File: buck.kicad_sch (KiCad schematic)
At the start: 35 parts, among them J6 Conn_01x02_Socket, Q3 BSC059N04LS6, Q4 BSC059N04LS6, U6 BQ24640

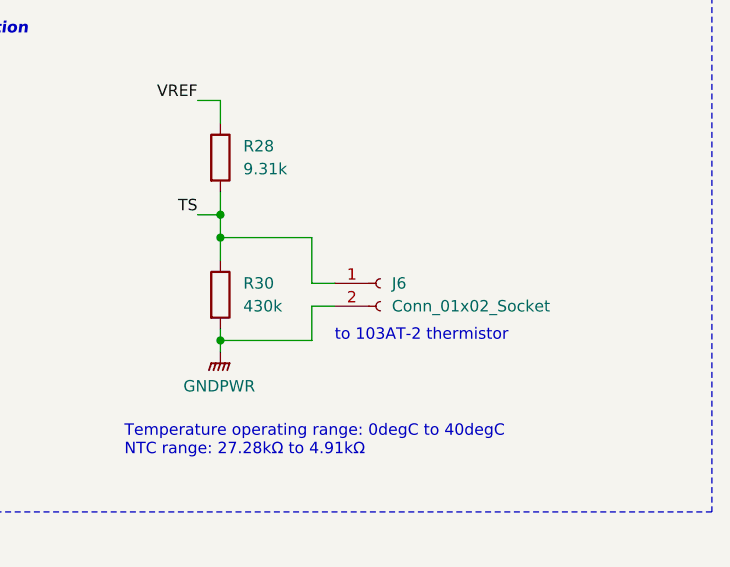
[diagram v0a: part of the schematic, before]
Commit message: Renumbering components
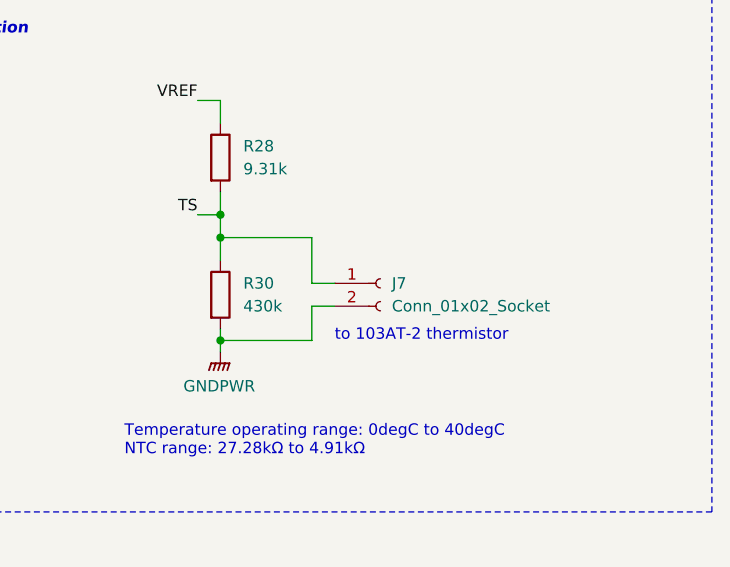
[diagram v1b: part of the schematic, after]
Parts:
- renumbered J6 to J7
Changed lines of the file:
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@@
 		(dnp no)
 		(fields_autoplaced yes)
-		(property "Reference" "#PWR035"
+		(property "Reference" "#PWR037"
 			(at 193.04 86.36 0)
 			(effects
@@
 			(project "SupercapManager"
 				(path "/6197145b-e7d4-44cc-9d90-537b6501bf60/388608c4-ca49-4b14-9684-8f150e280879"
-					(reference "#PWR035")
+					(reference "#PWR037")
 					(unit 1)
 				)
@@
 		(dnp no)
 		(fields_autoplaced yes)
-		(property "Reference" "#PWR040"
+		(property "Reference" "#PWR042"
 			(at 95.25 102.87 0)
 			(effects
@@
 			(project "SupercapManager"
 				(path "/6197145b-e7d4-44cc-9d90-537b6501bf60/388608c4-ca49-4b14-9684-8f150e280879"
-					(reference "#PWR040")
+					(reference "#PWR042")
 					(unit 1)
 				)
@@
 		(dnp no)
 		(fields_autoplaced yes)
-		(property "Reference" "#PWR043"
+		(property "Reference" "#PWR045"
 			(at 123.19 151.13 0)
 			(effects
@@
 			(project "SupercapManager"
 				(path "/6197145b-e7d4-44cc-9d90-537b6501bf60/388608c4-ca49-4b14-9684-8f150e280879"
-					(reference "#PWR043")
+					(reference "#PWR045")
 					(unit 1)
 				)
@@
 		(dnp no)
 		(fields_autoplaced yes)
-		(property "Reference" "#PWR042"
+		(property "Reference" "#PWR044"
 			(at 226.06 148.59 0)
 			(effects
@@
 			(project "SupercapManager"
 				(path "/6197145b-e7d4-44cc-9d90-537b6501bf60/388608c4-ca49-4b14-9684-8f150e280879"
-					(reference "#PWR042")
+					(reference "#PWR044")
 					(unit 1)
 				)
@@
 		(dnp no)
 		(fields_autoplaced yes)
-		(property "Reference" "#PWR041"
+		(property "Reference" "#PWR043"
 			(at 67.31 135.89 0)
 			(effects
@@
 			(project ""
 				(path "/6197145b-e7d4-44cc-9d90-537b6501bf60/388608c4-ca49-4b14-9684-8f150e280879"
-					(reference "#PWR041")
+					(reference "#PWR043")
 					(unit 1)
 				)
@@
 		(dnp no)
 		(fields_autoplaced yes)
-		(property "Reference" "J6"
+		(property "Reference" "J7"
 			(at 245.11 135.8899 0)
 			(effects
@@
 			(project ""
 				(path "/6197145b-e7d4-44cc-9d90-537b6501bf60/388608c4-ca49-4b14-9684-8f150e280879"
-					(reference "J6")
+					(reference "J7")
 					(unit 1)
 				)
@@
 		(dnp no)
 		(fields_autoplaced yes)
-		(property "Reference" "#PWR038"
+		(property "Reference" "#PWR040"
 			(at 46.99 100.33 0)
 			(effects
@@
 			(project "SupercapManager"
 				(path "/6197145b-e7d4-44cc-9d90-537b6501bf60/388608c4-ca49-4b14-9684-8f150e280879"
-					(reference "#PWR038")
+					(reference "#PWR040")
 					(unit 1)
 				)
@@
 		(dnp no)
 		(fields_autoplaced yes)
-		(property "Reference" "#PWR039"
+		(property "Reference" "#PWR041"
 			(at 232.41 101.6 0)
 			(effects
@@
 			(project "SupercapManager"
 				(path "/6197145b-e7d4-44cc-9d90-537b6501bf60/388608c4-ca49-4b14-9684-8f150e280879"
-					(reference "#PWR039")
+					(reference "#PWR041")
 					(unit 1)
 				)
@@
 		(dnp no)
 		(fields_autoplaced yes)
-		(property "Reference" "#PWR033"
+		(property "Reference" "#PWR035"
 			(at 127 52.07 0)
 			(effects
@@
 			(project "SupercapManager"
 				(path "/6197145b-e7d4-44cc-9d90-537b6501bf60/388608c4-ca49-4b14-9684-8f150e280879"
-					(reference "#PWR033")
+					(reference "#PWR035")
 					(unit 1)
 				)
@@
 		(dnp no)
 		(fields_autoplaced yes)
-		(property "Reference" "#PWR034"
+		(property "Reference" "#PWR036"
 			(at 41.91 55.88 0)
 			(effects
@@
 			(project "SupercapManager"
 				(path "/6197145b-e7d4-44cc-9d90-537b6501bf60/388608c4-ca49-4b14-9684-8f150e280879"
-					(reference "#PWR034")
+					(reference "#PWR036")
 					(unit 1)
 				)
@@
 		(dnp no)
 		(fields_autoplaced yes)
-		(property "Reference" "#PWR037"
+		(property "Reference" "#PWR039"
 			(at 176.53 88.9 0)
 			(effects
@@
 			(project "SupercapManager"
 				(path "/6197145b-e7d4-44cc-9d90-537b6501bf60/388608c4-ca49-4b14-9684-8f150e280879"
-					(reference "#PWR037")
+					(reference "#PWR039")
 					(unit 1)
 				)
@@
 		(dnp no)
 		(fields_autoplaced yes)
-		(property "Reference" "#PWR036"
+		(property "Reference" "#PWR038"
 			(at 148.59 88.9 0)
 			(effects
@@
 			(project "SupercapManager"
 				(path "/6197145b-e7d4-44cc-9d90-537b6501bf60/388608c4-ca49-4b14-9684-8f150e280879"
-					(reference "#PWR036")
+					(reference "#PWR038")
 					(unit 1)
 				)

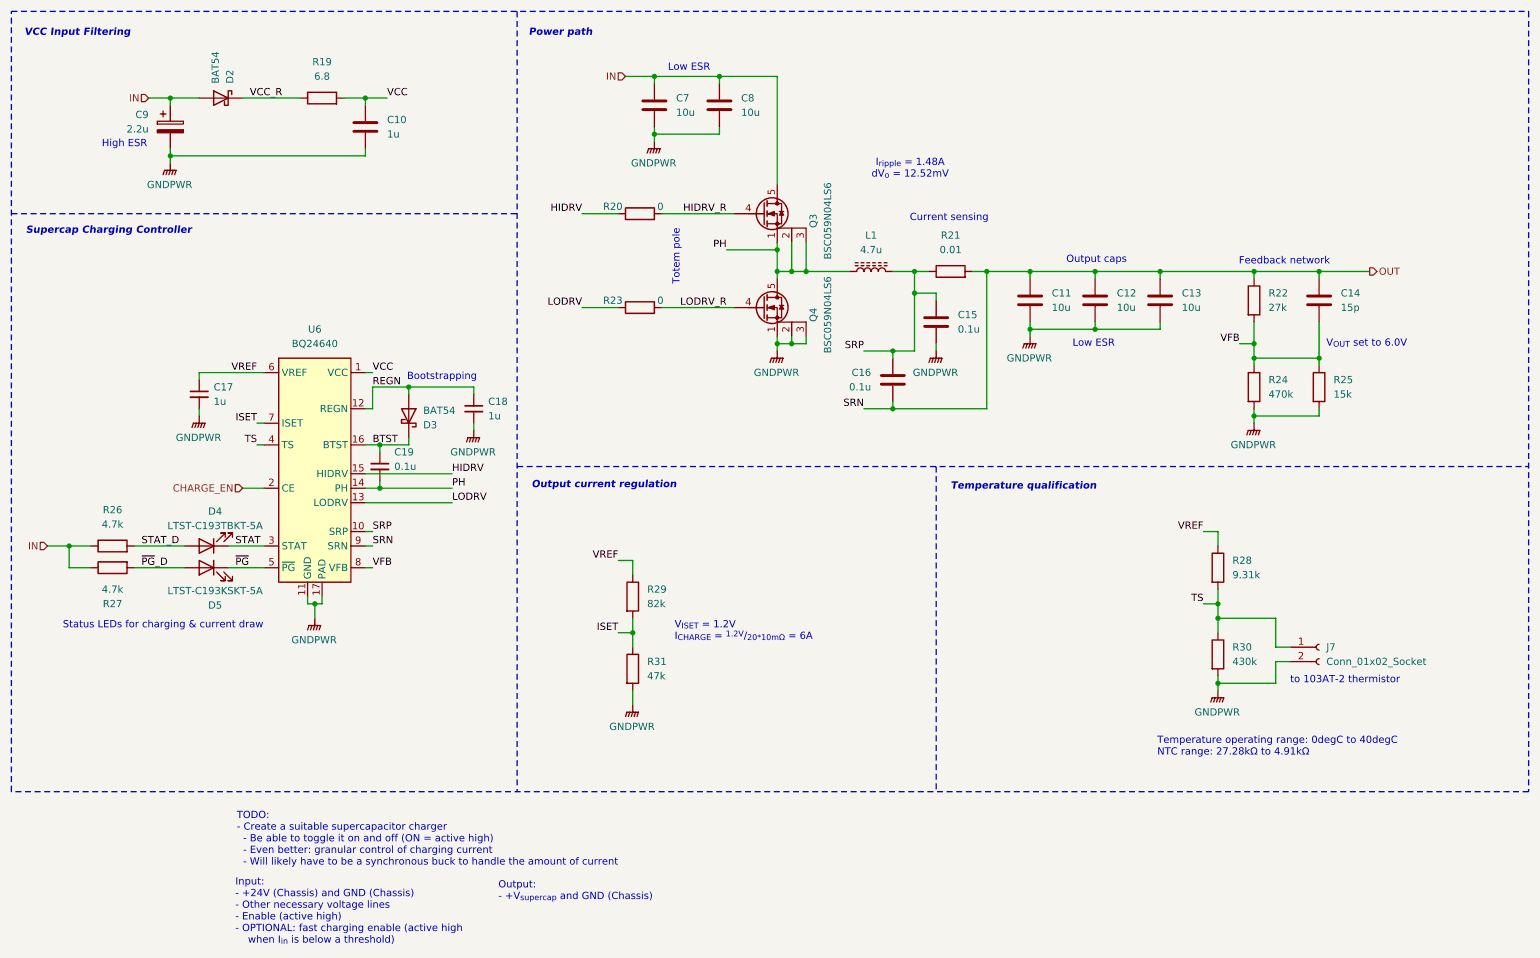
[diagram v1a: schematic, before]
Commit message: Add voltage ratings to capacitors & respec caps to not explode
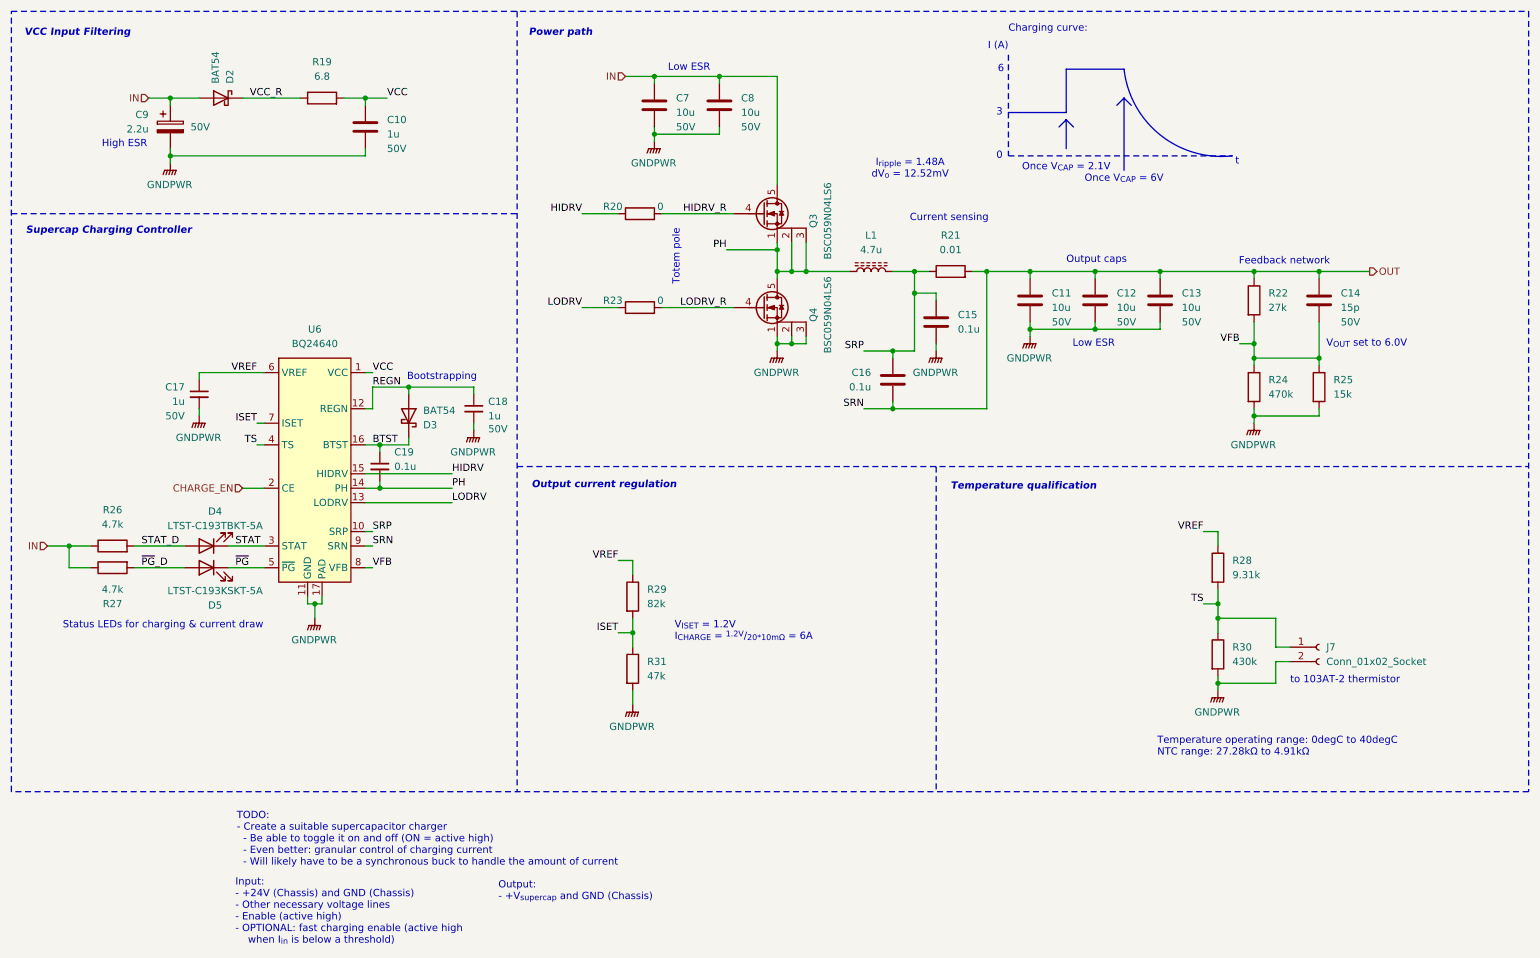
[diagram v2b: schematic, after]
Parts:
- C10, C17, C18: Mouser Part Number 80-C0603C105K9PLR -> 963-UMK107BJ105KA-T; Voltage Rating (none) -> 50V
- C11, C12, C13, C7, C8: footprint Capacitor_SMD:C_0805_2012Metric_Pad1.18x1.45mm_HandSolder -> Capacitor_SMD:C_1206_3216Metric_Pad1.33x1.80mm_HandSolder; Mouser Part Number 187-CL21A106KAYNNNE -> 187-CL31A106KBHNNNE; Voltage Rating (none) -> 50V
- C14, C9: Voltage Rating (none) -> 50V
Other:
- note added: "0"
- note added: "3"
- note added: "6"
- note added: "Charging curve:"
- note added: "I (A)"
- note added: "Once V_{CAP} = 2.1V"
- note added: "Once V_{CAP} = 6V"
- note added: "t"

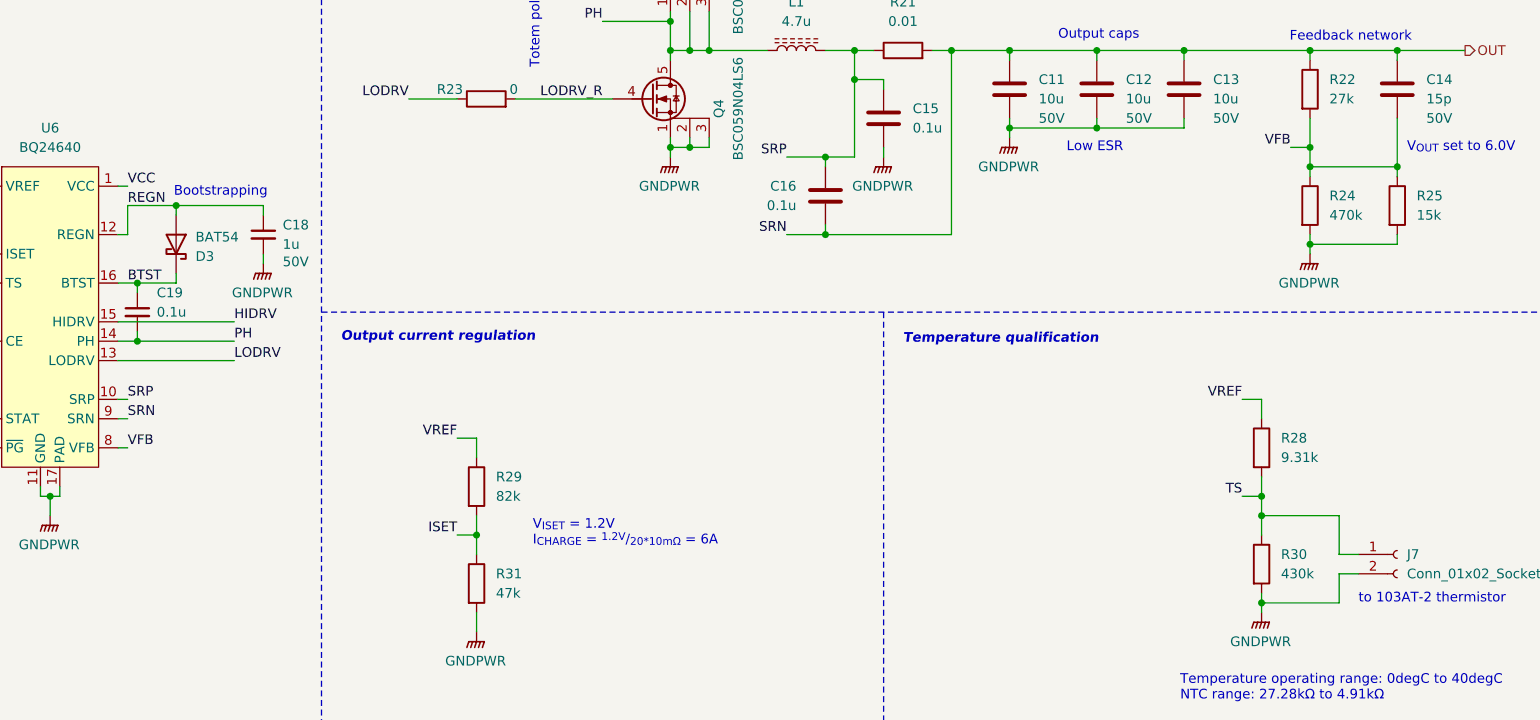
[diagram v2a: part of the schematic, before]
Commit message: Specc'd all components + started creating rev 1b boards
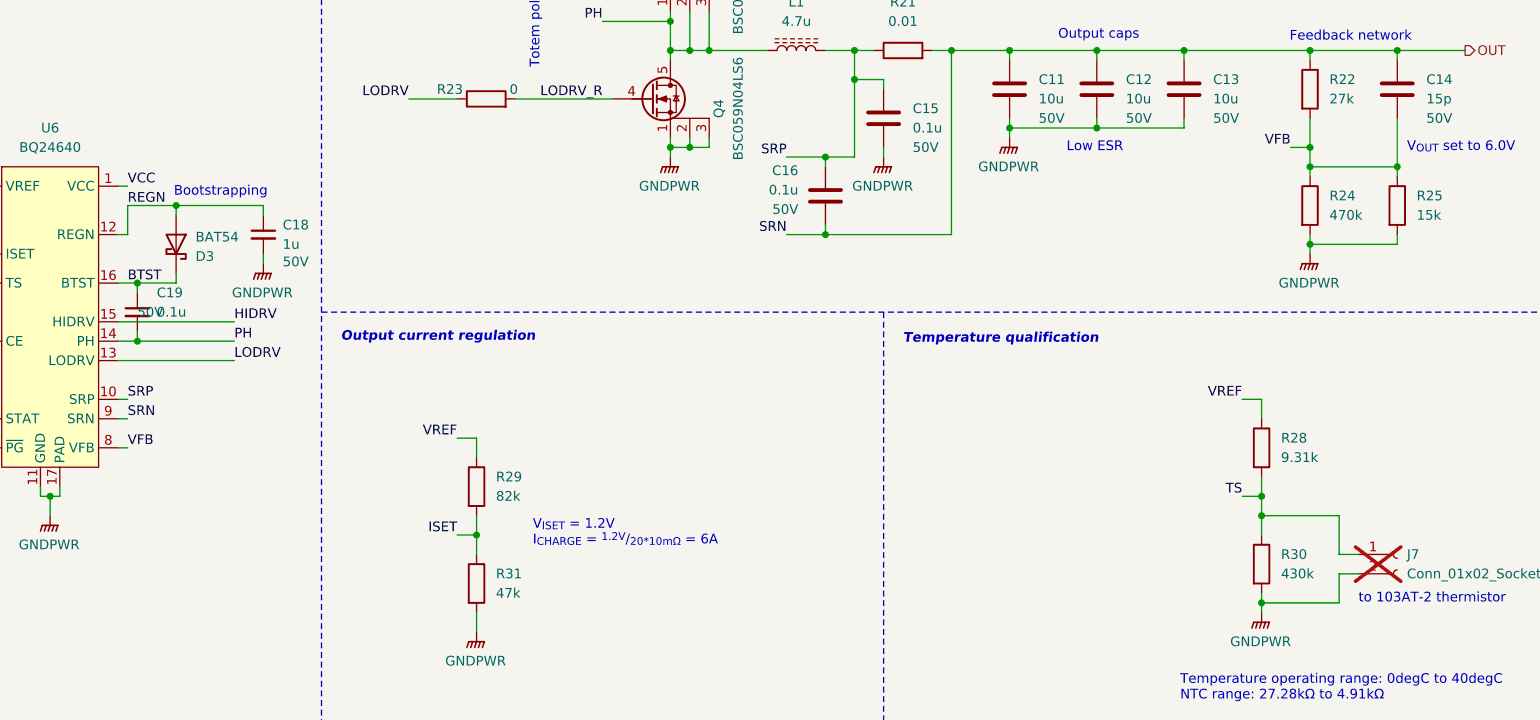
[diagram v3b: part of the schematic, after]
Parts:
- C15, C16, C19: Mouser Part Number (none) -> 581-KGM15BR71H104JT; Voltage Rating (none) -> 50V
- J7: now not fitted
- R19: footprint Resistor_SMD:R_0603_1608Metric_Pad0.98x0.95mm_HandSolder -> Resistor_SMD:R_0805_2012Metric_Pad1.20x1.40mm_HandSolder; Mouser Part Number (none) -> 660-RK73B2ATTD6R8J
- R20, R23: Mouser Part Number (none) -> 660-RK73Z1JTTDD
- R22: Mouser Part Number 667-ERA-3AEB204V -> 660-RN73H1JTD2702B25
- R24: Mouser Part Number 603-RT0603BRD07280KL -> 660-RN73R1JTD4703B25
- R25: Mouser Part Number 603-RC0603FR-071M05L -> 603-RT0603FRE1315KL
- R26, R27: Mouser Part Number 603-RT0603FRE133K6L -> 660-RN73R1JTD4701F50
- R28: Mouser Part Number (none) -> 603-RT0603DRE079K31L
- R29: Mouser Part Number (none) -> 603-RT0603FRE0782KL
- R30: Mouser Part Number (none) -> 603-RT0603FRE07430KL
- R31: Mouser Part Number (none) -> 603-RC0603FR-1047KL
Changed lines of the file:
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@@
 			)
 		)
-		(property "Mouser Part Number" "667-ERA-3AEB204V"
+		(property "Mouser Part Number" "660-RN73H1JTD2702B25"
 			(at 232.41 74.93 0)
 			(effects
@@
 			)
 		)
+		(property "Mouser Part Number" "603-RT0603FRE07430KL"
+			(at 226.06 137.16 0)
+			(effects
+				(font
+					(size 1.27 1.27)
+				)
+				(hide yes)
+			)
+		)
 		(pin "1"
 		)
@@
 			)
 		)
+		(property "Mouser Part Number" "660-RK73Z1JTTDD"
+			(at 124.46 59.69 0)
+			(effects
+				(font
+					(size 1.27 1.27)
+				)
+				(hide yes)
+			)
+		)
 		(pin "2"
 		)
@@
 			)
 		)
-		(property "Footprint" "Resistor_SMD:R_0603_1608Metric_Pad0.98x0.95mm_HandSolder"
+		(property "Footprint" "Resistor_SMD:R_0805_2012Metric_Pad1.20x1.40mm_HandSolder"
 			(at 68.58 41.148 90)
 			(effects
@@
 			)
 		)
+		(property "Mouser Part Number" "660-RK73B2ATTD6R8J"
+			(at 68.58 39.37 0)
+			(effects
+				(font
+					(size 1.27 1.27)
+				)
+				(hide yes)
+			)
+		)
 		(pin "1"
 		)
@@
 			)
 		)
-		(property "Mouser Part Number" "603-RT0603FRE133K6L"
+		(property "Mouser Part Number" "660-RN73R1JTD4701F50"
 			(at 31.75 121.92 0)
 			(effects
@@
 			)
 		)
-		(property "Mouser Part Number" "603-RC0603FR-071M05L"
+		(property "Mouser Part Number" "603-RT0603FRE1315KL"
 			(at 243.84 90.17 0)
 			(effects
@@
 			)
 		)
+		(property "Mouser Part Number" "660-RK73Z1JTTDD"
+			(at 124.46 76.2 0)
+			(effects
+				(font
+					(size 1.27 1.27)
+				)
+				(hide yes)
+			)
+		)
 		(pin "2"
 		)
@@
 		(in_bom yes)
 		(on_board yes)
-		(dnp no)
+		(dnp yes)
 		(fields_autoplaced yes)
 		(property "Reference" "J7"
@@
 			)
 		)
+		(property "Mouser Part Number" "603-RC0603FR-1047KL"
+			(at 123.19 139.7 0)
+			(effects
+				(font
+					(size 1.27 1.27)
+				)
+				(hide yes)
+			)
+		)
 		(pin "2"
 		)
@@
 			)
 		)
+		(property "Mouser Part Number" "603-RT0603DRE079K31L"
+			(at 226.06 121.92 0)
+			(effects
+				(font
+					(size 1.27 1.27)
+				)
+				(hide yes)
+			)
+		)
 		(pin "1"
 		)
@@
 			)
 		)
+		(property "Mouser Part Number" "603-RT0603FRE0782KL"
+			(at 123.19 127 0)
+			(effects
+				(font
+					(size 1.27 1.27)
+				)
+				(hide yes)
+			)
+		)
 		(pin "2"
 		)
@@
 		(dnp no)
 		(property "Reference" "C16"
-			(at 165.1 87.6299 0)
+			(at 165.354 85.598 0)
 			(effects
 				(font
@@
 		)
 		(property "Value" "0.1u"
-			(at 165.1 90.1699 0)
+			(at 165.354 88.138 0)
 			(effects
 				(font
@@
 			)
 		)
-		(property "Datasheet" "~"
+		(property "Datasheet" "https://www.mouser.com/datasheet/2/40/KGM_X7R-3223212.pdf"
 			(at 168.91 88.9 0)
 			(effects
@@
 			)
 		)
+		(property "Mouser Part Number" "581-KGM15BR71H104JT"
+			(at 168.91 88.9 0)
+			(effects
+				(font
+					(size 1.27 1.27)
+				)
+				(hide yes)
+			)
+		)
+		(property "Voltage Rating" "50V"
+			(at 165.354 90.6781 0)
+			(effects
+				(font
+					(size 1.27 1.27)
+				)
+				(justify left)
+			)
+		)
 		(pin "2"
 		)
@@
 		(on_board yes)
 		(dnp no)
-		(fields_autoplaced yes)
 		(property "Reference" "C15"
 			(at 180.34 77.4699 0)
@@
 			)
 		)
-		(property "Datasheet" "~"
+		(property "Datasheet" "https://www.mouser.com/datasheet/2/40/KGM_X7R-3223212.pdf"
 			(at 176.53 78.74 0)
 			(effects
@@
 			)
 		)
+		(property "Mouser Part Number" "581-KGM15BR71H104JT"
+			(at 176.53 78.74 0)
+			(effects
+				(font
+					(size 1.27 1.27)
+				)
+				(hide yes)
+			)
+		)
+		(property "Voltage Rating" "50V"
+			(at 180.34 82.55 0)
+			(effects
+				(font
+					(size 1.27 1.27)
+				)
+				(justify left)
+			)
+		)
 		(pin "2"
 		)
@@
 			)
 		)
-		(property "Mouser Part Number" "603-RT0603BRD07280KL"
+		(property "Mouser Part Number" "660-RN73R1JTD4703B25"
 			(at 232.41 90.17 0)
 			(effects
@@
 			)
 		)
-		(property "Mouser Part Number" "603-RT0603FRE133K6L"
+		(property "Mouser Part Number" "660-RN73R1JTD4701F50"
 			(at 31.75 118.11 0)
 			(effects
@@
 			)
 		)
-		(property "Datasheet" "~"
+		(property "Datasheet" "https://www.mouser.com/datasheet/2/40/KGM_X7R-3223212.pdf"
 			(at 78.74 104.14 0)
 			(effects
@@
 			)
 		)
+		(property "Mouser Part Number" "581-KGM15BR71H104JT"
+			(at 78.74 104.14 0)
+			(effects
+				(font
+					(size 1.27 1.27)
+				)
+				(hide yes)
+			)
+		)
+		(property "Voltage Rating" "50V"
+			(at 78.74 104.14 0)
+			(effects
+				(font
+					(size 1.27 1.27)
+				)
+				(justify left)
+			)
+		)
